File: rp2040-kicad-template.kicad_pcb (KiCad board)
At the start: 2 copper layers, 40 x 40 mm, 42 parts, among them U10 PJ-320A, U11 RP2040, U12 XC6206PxxxMR, U13 USB Boot, U14 USBLC6-2SC6, U15 Reset, U16 W25Q16JVUXIQ, U9 TYPE-C-31-M-12, Y2 12MHz - 20pF

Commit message: Progress on the PCB layout
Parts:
- moved U12 62.3 mm to (188.5, 86.7)
- moved D1 52.4 mm to (193.2, 90.9)
- moved F2 51.1 mm to (192.5, 88.6)
- moved FB2 44.8 mm to (192.5, 86.6), turned to 180 degrees
- moved C23 42.5 mm to (189.7, 84.4), turned to 180 degrees
- moved C24 38.8 mm to (185.9, 87.2), turned to 90 degrees
- moved C27 2.47 mm to (200.0, 71.9), turned to 90 degrees
- moved C25 2.43 mm to (205.2, 71.9), turned to -90 degrees
- moved R14 0.59 mm to (200.0, 73.8)

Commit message: Progress on the PCB layout
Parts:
- moved U13 82.3 mm to (211.2, 90.8), turned to 180 degrees
- moved U15 70.5 mm to (196.3, 69.6), turned to 90 degrees
- moved R18 64.5 mm to (208.3, 86.6), turned to -90 degrees
- moved R15 62.6 mm to (206.1, 89.0), turned to -90 degrees
- moved C21 61.2 mm to (197.0, 83.8), turned to 180 degrees
- moved C22 61.2 mm to (197.0, 84.8), turned to 180 degrees
- moved R17 57.0 mm to (196.3, 63.2), turned to 180 degrees
- moved C33 56.0 mm to (205.5, 78.2)
- moved C34 55.3 mm to (205.1, 82.4), turned to -90 degrees
- moved C26 53.9 mm to (196.3, 64.3), turned to 180 degrees
- moved C36 51.3 mm to (201.0, 85.9)
- moved C35 51.2 mm to (201.0, 84.9)
- moved C32 50.6 mm to (199.6, 74.0), turned to 90 degrees
- moved R1 50.4 mm to (208.7, 82.9), turned to -90 degrees
- moved C30 49.5 mm to (195.5, 81.3), turned to 90 degrees
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
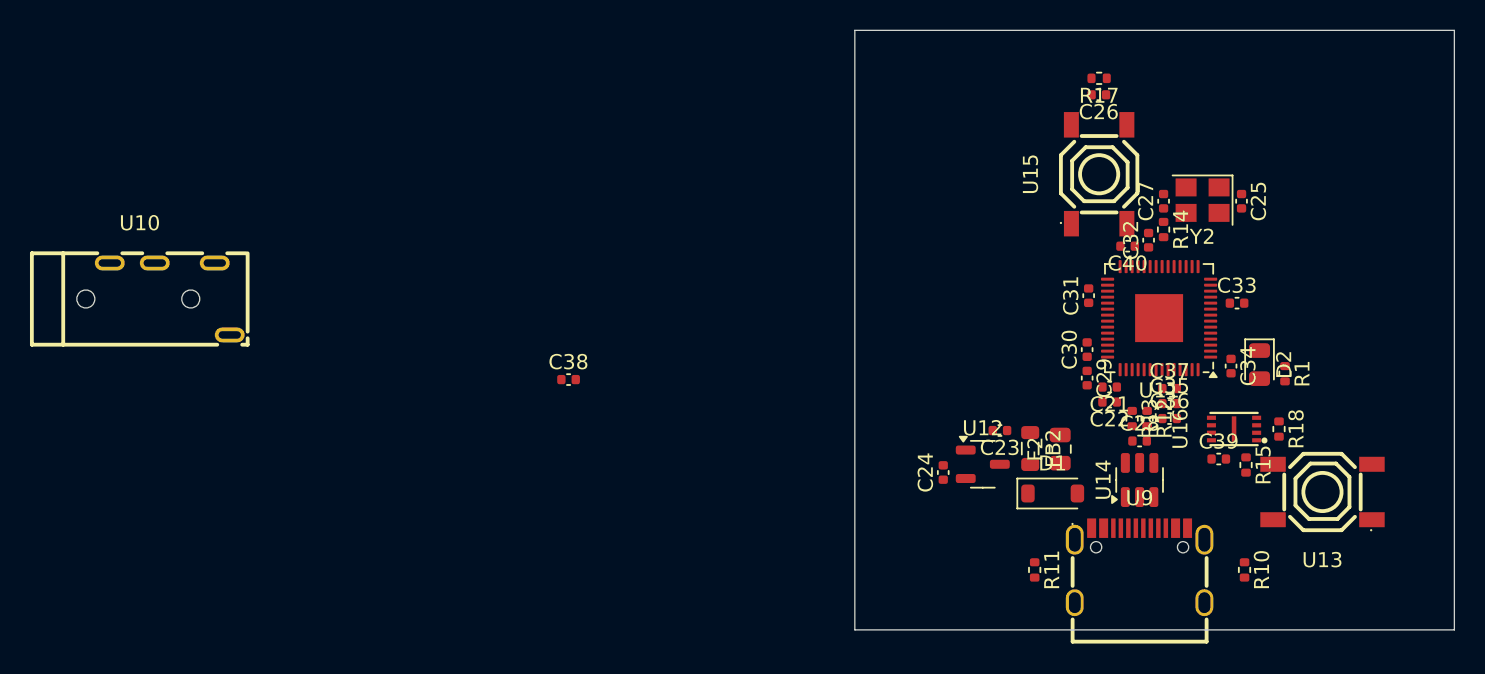
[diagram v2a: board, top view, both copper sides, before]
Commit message: Replace the SWD TRRS connector with a simple header pin connector
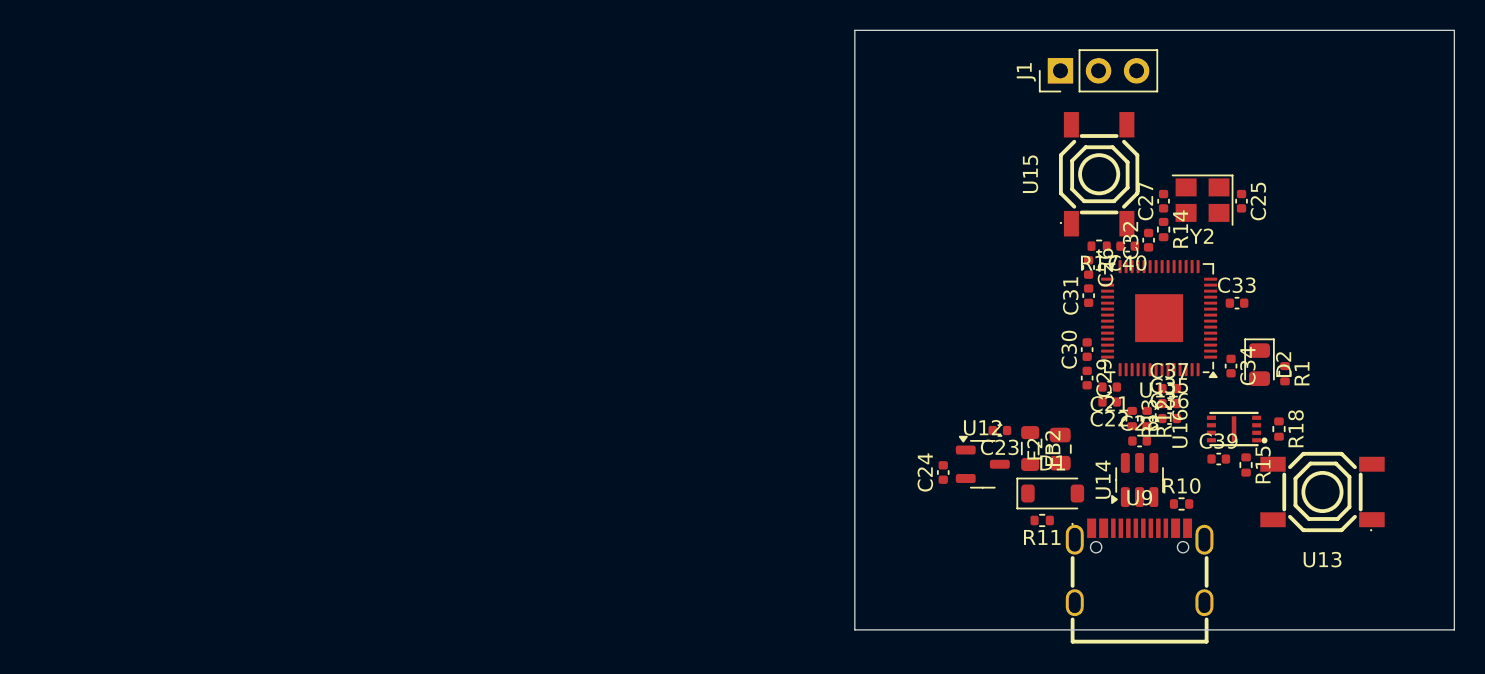
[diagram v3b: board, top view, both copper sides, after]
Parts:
- removed C38: 100nF, Capacitor_SMD:C_0402_1005Metric
- removed U10: PJ-320A, footprints:trrs-connector-pj320a
- added J1: Conn_01x03, Connector_PinHeader_2.54mm:PinHeader_1x03_P2.54mm_Vertical, F.Cu at (193.7, 62.7)
- moved C26 11.5 mm to (195.6, 75.8), turned to -90 degrees
- moved R17 11.2 mm to (196.3, 74.4)
- moved R10 6.08 mm to (201.8, 91.6), turned to 0 degrees
- moved R11 3.34 mm to (192.5, 92.7), turned to 180 degrees

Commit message: Start some routing
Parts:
- moved C24 5.31 mm to (189.5, 85.6), turned to 0 degrees
- moved C23 4.20 mm to (189.5, 90.9), turned to 0 degrees
- moved C35 1.00 mm to (201.0, 85.9)
- moved C36 1.00 mm to (201.0, 86.9)
- moved C37 1.00 mm to (201.0, 84.9)
- moved U12 0.88 mm to (189.0, 88.2), turned to -90 degrees
- moved U15 0.35 mm to (196.3, 69.2)
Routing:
- net /rp2040/VBUS: track 0.00 -> 11.1 mm
- net +5V: track 0.00 -> 4.43 mm
- net Net-(D1-K): track 0.00 -> 3.65 mm
- net +3V3: track 0.00 -> 2.16 mm
- net Net-(F2-Pad2): track 0.00 -> 2.07 mm
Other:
- board text added: "Boot"
- board text added: "Reset"

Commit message: More routing
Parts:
- moved R11 5.31 mm to (196.4, 89.1), turned to 90 degrees
- moved C27 4.80 mm to (203.4, 67.5), turned to 0 degrees
- moved R15 3.77 mm to (209.3, 87.0)
- moved C39 3.25 mm to (207.1, 87.0), turned to 90 degrees
- moved U13 2.69 mm to (208.8, 91.9)
- moved R1 2.55 mm to (206.2, 82.4)
- moved R10 2.50 mm to (201.6, 89.1), turned to 90 degrees
- moved R17 2.33 mm to (194.0, 74.8), turned to -90 degrees
- moved D2 1.32 mm to (208.3, 82.5)
- moved Y2 1.15 mm to (203.4, 70.2), turned to 90 degrees
- moved C26 1.14 mm to (195.1, 74.8)
- moved C25 1.10 mm to (205.8, 70.3), turned to 90 degrees
- moved R18 0.41 mm to (208.2, 87.0), turned to 90 degrees
- moved C32 0.40 mm to (200.0, 74.0)
- moved C40 0.40 mm to (198.6, 74.4)
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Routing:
- net +3V3: track 2.16 -> 118.4 mm
- net (no net): track 0.00 -> 20.0 mm, vias 0 -> 17
- net +1V1: track 0.00 -> 17.9 mm
- net QSPI_SD3: track 0.00 -> 10.4 mm
- net QSPI_SCLK: track 0.00 -> 8.70 mm
- net /rp2040/USB-: track 0.00 -> 8.25 mm
- net /rp2040/QSPI_SS: track 0.00 -> 8.20 mm
- net /rp2040/USB+: track 0.00 -> 7.20 mm
- net QSPI_SD0: track 0.00 -> 6.54 mm
- net /rp2040/OSC_OUT: track 0.00 -> 6.08 mm
- net /rp2040/QSPI_SD1: track 0.00 -> 4.39 mm
- net /rp2040/OSC_IN: track 0.00 -> 4.32 mm
- net /rp2040/QSPI_SD2: track 0.00 -> 4.31 mm
- net Net-(U13-C): track 0.00 -> 4.21 mm
- net /rp2040/CC1: track 0.00 -> 4.16 mm
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
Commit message: More routing
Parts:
- moved J1 2.59 mm to (192.4, 64.9)
- moved R10 2.01 mm to (201.4, 91.1)
- moved U15 1.50 mm to (194.9, 69.8), turned to 0 degrees
- moved C40 0.98 mm to (199.0, 73.5), turned to 90 degrees
- moved C24 0.90 mm to (188.6, 85.6)
- moved C32 0.50 mm to (200.0, 73.5)
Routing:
- net /rp2040/SWD: track 0.00 -> 15.1 mm
- net /rp2040/SWCLK: track 0.00 -> 13.2 mm
- net /rp2040/RUN: track 0.00 -> 9.53 mm
- net GND: track 1.12 -> 6.49 mm, vias 6 -> 7
- net /USER_LED: track 0.00 -> 4.63 mm
- net (no net): track 20.0 -> 22.6 mm, vias 17 -> 19
- net /rp2040/CC2: track 3.96 -> 1.88 mm
- net /rp2040/OSC_OUT: track 6.08 -> 8.14 mm
- net /rp2040/OSC_IN: track 4.32 -> 6.08 mm
- net +3V3: track 118.4 -> 117.0 mm
